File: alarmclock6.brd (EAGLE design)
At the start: 60 x 92 mm, 51 parts, among them Q1 FDN360P, T1 2N2222, X1 MKDSN1,5/2-5,08, X2 MKDSN1,5/2-5,08, X3 MKDSN1,5/2-5,08, X4 MKDSN1,5/2-5,08

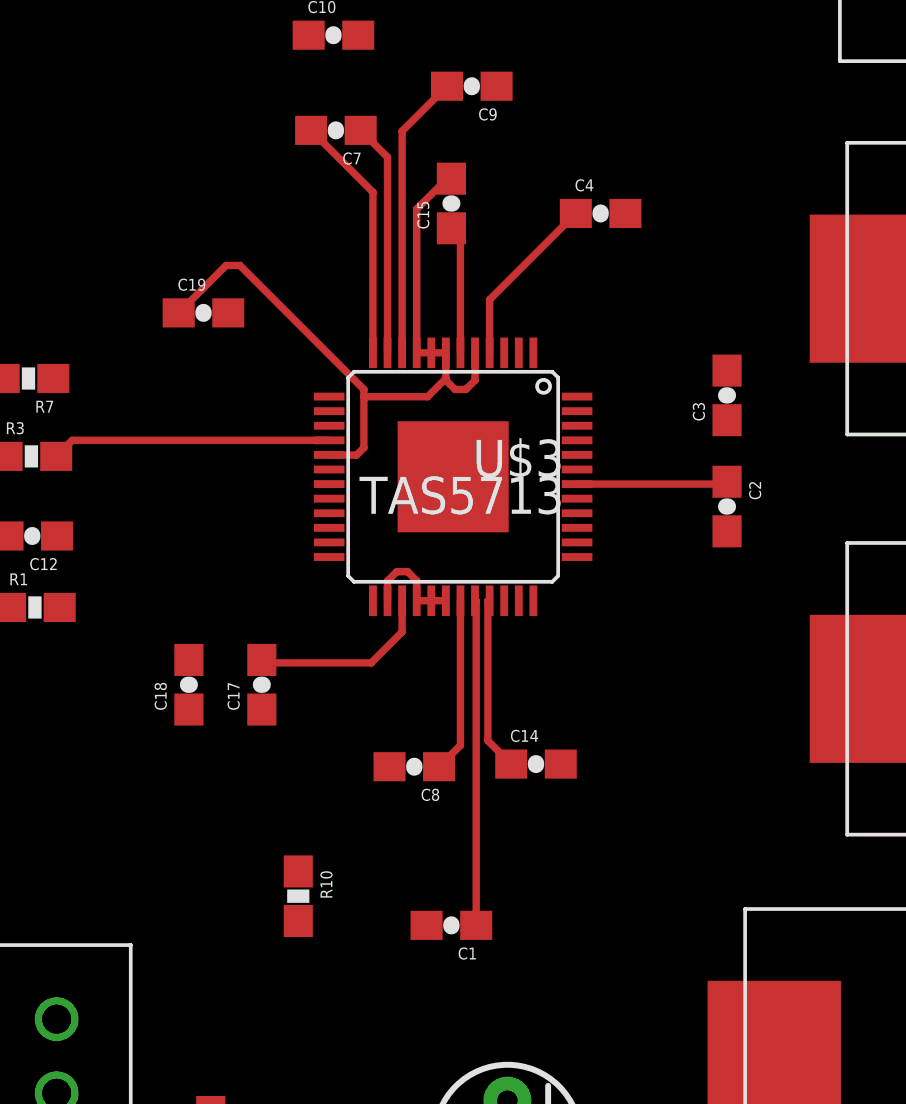
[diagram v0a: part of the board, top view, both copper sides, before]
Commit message: bugfix on DC-DC converter
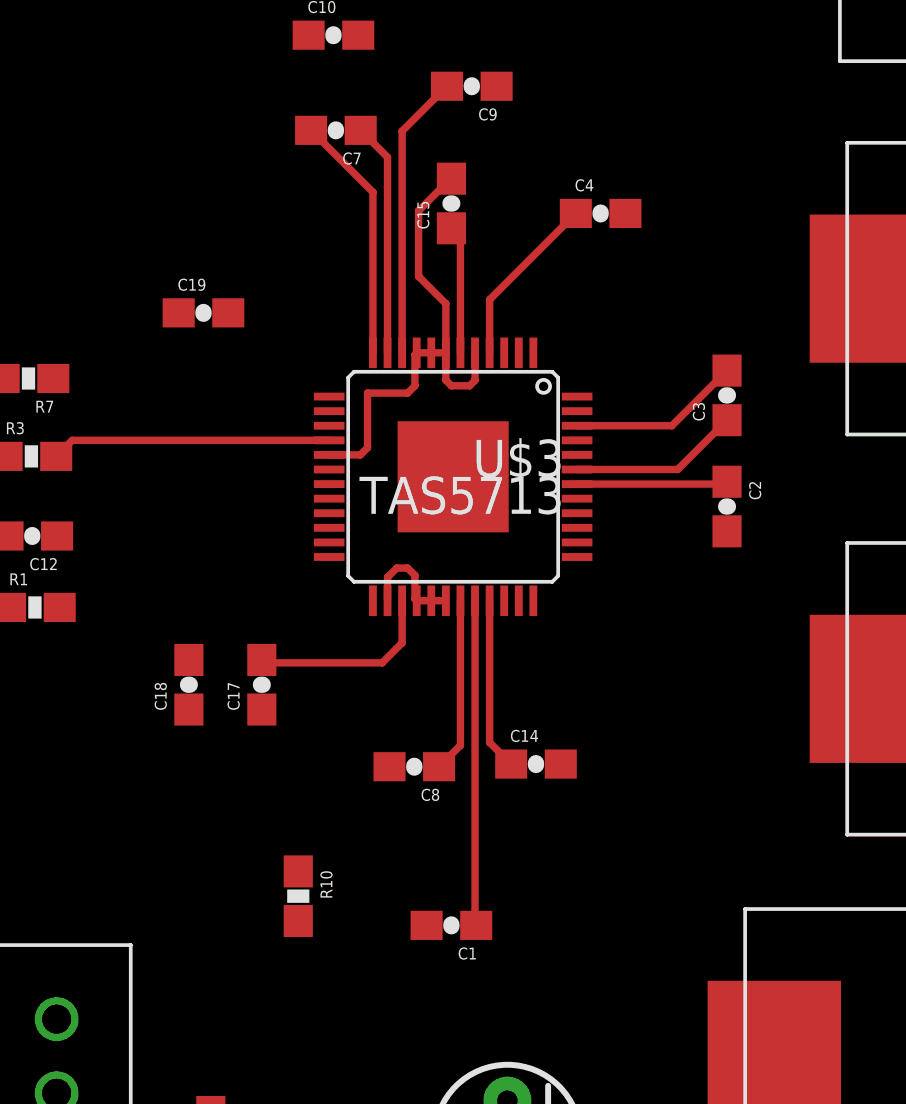
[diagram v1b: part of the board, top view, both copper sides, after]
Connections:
- net N$3: now also U$14.VOUT; no longer U$14.VIN
- net N$43: now also U$14.VIN; no longer U$14.VOUT
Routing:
- net GND: track 29.5 -> 20.9 mm
- net N$14: track 0.00 -> 5.92 mm
- net N$15: track 0.00 -> 5.84 mm
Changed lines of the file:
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@@
 <contactref element="U$4" pad="P$1"/>
 <contactref element="C11" pad="1"/>
-<contactref element="U$14" pad="VIN"/>
-<wire x1="25.17" y1="17.7" x2="5.46" y2="68.75" width="0" layer="19" extent="1-1"/>
+<contactref element="U$14" pad="VOUT"/>
+<wire x1="25.17" y1="17.7" x2="10.54" y2="68.75" width="0" layer="19" extent="1-1"/>
 <wire x1="48.024" y1="13.018" x2="25.17" y2="17.7" width="0" layer="19" extent="1-1"/>
 </signal>
@@
 <contactref element="C11" pad="2"/>
 <contactref element="U$14" pad="GND"/>
-<wire x1="22.06" y1="37.38" x2="22.06" y2="38.065" width="0.254" layer="1"/>
-<wire x1="22.06" y1="38.065" x2="21.75" y2="38.375" width="0.254" layer="1"/>
-<wire x1="21.75" y1="38.375" x2="21.375" y2="38.375" width="0.254" layer="1"/>
-<wire x1="21.375" y1="38.375" x2="21.06" y2="38.06" width="0.254" layer="1"/>
-<wire x1="21.06" y1="38.06" x2="21.06" y2="37.38" width="0.254" layer="1"/>
-<wire x1="23.25" y1="51.85" x2="23.1" y2="51.85" width="0.254" layer="1"/>
-<wire x1="23.1" y1="51.85" x2="22.06" y2="50.81" width="0.254" layer="1"/>
-<wire x1="22.06" y1="50.81" x2="22.06" y2="45.88" width="0.254" layer="1"/>
-<wire x1="23.06" y1="45.88" x2="22.56" y2="45.88" width="0.254" layer="1"/>
-<wire x1="22.56" y1="45.88" x2="22.06" y2="45.88" width="0.254" layer="1"/>
-<wire x1="23.06" y1="45.88" x2="23.06" y2="45" width="0.254" layer="1"/>
-<wire x1="23.06" y1="45" x2="23.06" y2="44.94" width="0.254" layer="1"/>
-<wire x1="23.06" y1="44.94" x2="23.375" y2="44.625" width="0.254" layer="1"/>
-<wire x1="23.375" y1="44.625" x2="23.75" y2="44.625" width="0.254" layer="1"/>
-<wire x1="23.75" y1="44.625" x2="24.06" y2="44.935" width="0.254" layer="1"/>
-<wire x1="24.06" y1="44.935" x2="24.06" y2="45.88" width="0.254" layer="1"/>
-<wire x1="19.06" y1="42.38" x2="19.065" y2="42.375" width="0.254" layer="1"/>
-<wire x1="19.065" y1="42.375" x2="20" y2="42.375" width="0.254" layer="1"/>
-<wire x1="20" y1="42.375" x2="20.25" y2="42.625" width="0.254" layer="1"/>
-<wire x1="20.25" y1="42.625" x2="20.25" y2="44.375" width="0.254" layer="1"/>
-<wire x1="20.25" y1="44.375" x2="22.435" y2="44.375" width="0.254" layer="1"/>
-<wire x1="22.435" y1="44.375" x2="23.06" y2="45" width="0.254" layer="1"/>
 <wire x1="33.6" y1="65.5" x2="37.77" y2="70.5" width="0" layer="19" extent="1-1"/>
 <wire x1="24.8" y1="55.02" x2="33.6" y2="65.5" width="0" layer="19" extent="1-1"/>
 <wire x1="23.25" y1="51.85" x2="24.8" y2="55.02" width="0" layer="19" extent="1-1"/>
-<wire x1="27.56" y1="44.38" x2="24.06" y2="44.935" width="0" layer="19" extent="1-1"/>
+<wire x1="27.56" y1="44.38" x2="24.06" y2="45.88" width="0" layer="19" extent="1-1"/>
 <wire x1="27.56" y1="43.88" x2="27.56" y2="44.38" width="0" layer="19" extent="1-1"/>
-<wire x1="21.375" y1="38.375" x2="20" y2="42.375" width="0" layer="19" extent="1-1"/>
 <wire x1="27.56" y1="39.38" x2="27.56" y2="43.88" width="0" layer="19" extent="1-1"/>
 <wire x1="27.56" y1="38.88" x2="27.56" y2="39.38" width="0" layer="19" extent="1-1"/>
+<wire x1="23.06" y1="37.38" x2="27.56" y2="38.88" width="0" layer="19" extent="1-1"/>
 <wire x1="21.128" y1="31.69" x2="21.06" y2="37.38" width="0" layer="19" extent="1-1"/>
 <wire x1="16.75" y1="33.65" x2="21.128" y2="31.69" width="0" layer="19" extent="1-1"/>
@@
 <wire x1="22.4" y1="26.25" x2="21.128" y2="31.69" width="0" layer="19" extent="1-1"/>
 <wire x1="25.17" y1="20.24" x2="22.4" y2="26.25" width="0" layer="19" extent="1-1"/>
+<wire x1="13.9" y1="47.25" x2="19.06" y2="42.38" width="0" layer="19" extent="1-1"/>
 <wire x1="7.9" y1="45" x2="13.9" y2="47.25" width="0" layer="19" extent="1-1"/>
 <wire x1="8" y1="42.33" x2="7.9" y2="45" width="0" layer="19" extent="1-1"/>
@@
 <wire x1="16.7551" y1="4.579" x2="29.4871" y2="4.579" width="0" layer="19" extent="1-1"/>
 <wire x1="48.024" y1="20.018" x2="25.17" y2="20.24" width="0" layer="19" extent="1-1"/>
-<wire x1="20.25" y1="44.375" x2="20.25" y2="44.625" width="0.254" layer="1"/>
-<wire x1="20.25" y1="44.625" x2="16" y2="48.875" width="0.254" layer="1"/>
-<wire x1="16" y1="48.875" x2="15.525" y2="48.875" width="0.254" layer="1"/>
-<wire x1="15.525" y1="48.875" x2="13.9" y2="47.25" width="0.254" layer="1"/>
-<wire x1="22.06" y1="37.38" x2="22.56" y2="37.38" width="0.254" layer="1"/>
+<wire x1="19.06" y1="42.38" x2="20.13" y2="42.38" width="0.254" layer="1"/>
+<wire x1="20.13" y1="42.38" x2="20.375" y2="42.625" width="0.254" layer="1"/>
+<wire x1="20.375" y1="42.625" x2="20.375" y2="44.5" width="0.254" layer="1"/>
+<wire x1="20.375" y1="44.5" x2="21.75" y2="44.5" width="0.254" layer="1"/>
+<wire x1="21.75" y1="44.5" x2="22" y2="44.75" width="0.254" layer="1"/>
+<wire x1="22" y1="44.75" x2="22" y2="45.82" width="0.254" layer="1"/>
+<wire x1="22" y1="45.82" x2="22.06" y2="45.88" width="0.254" layer="1"/>
+<wire x1="22.56" y1="45.88" x2="22.06" y2="45.88" width="0.254" layer="1"/>
+<wire x1="23.06" y1="45.88" x2="22.56" y2="45.88" width="0.254" layer="1"/>
+<wire x1="23.06" y1="45.88" x2="23.06" y2="44.94" width="0.254" layer="1"/>
+<wire x1="23.06" y1="44.94" x2="23.25" y2="44.75" width="0.254" layer="1"/>
+<wire x1="23.25" y1="44.75" x2="23.875" y2="44.75" width="0.254" layer="1"/>
+<wire x1="23.875" y1="44.75" x2="24.06" y2="44.935" width="0.254" layer="1"/>
+<wire x1="24.06" y1="44.935" x2="24.06" y2="45.88" width="0.254" layer="1"/>
+<wire x1="23.06" y1="45.88" x2="23.06" y2="47.565" width="0.254" layer="1"/>
+<wire x1="23.06" y1="47.565" x2="22.125" y2="48.5" width="0.254" layer="1"/>
+<wire x1="22.125" y1="48.5" x2="22.125" y2="50.75" width="0.254" layer="1"/>
+<wire x1="22.125" y1="50.75" x2="23.225" y2="51.85" width="0.254" layer="1"/>
+<wire x1="23.225" y1="51.85" x2="23.25" y2="51.85" width="0.254" layer="1"/>
+<wire x1="21.06" y1="37.38" x2="21.06" y2="38.185" width="0.254" layer="1"/>
+<wire x1="21.06" y1="38.185" x2="21.375" y2="38.5" width="0.254" layer="1"/>
+<wire x1="21.375" y1="38.5" x2="21.75" y2="38.5" width="0.254" layer="1"/>
+<wire x1="21.75" y1="38.5" x2="22" y2="38.25" width="0.254" layer="1"/>
+<wire x1="22" y1="38.25" x2="22" y2="37.44" width="0.254" layer="1"/>
+<wire x1="22" y1="37.44" x2="22.06" y2="37.38" width="0.254" layer="1"/>
+<wire x1="22.56" y1="37.38" x2="22.06" y2="37.38" width="0.254" layer="1"/>
 <wire x1="22.56" y1="37.38" x2="23.06" y2="37.38" width="0.254" layer="1"/>
 </signal>
@@
 <contactref element="U$3" pad="P$33"/>
 <contactref element="C14" pad="1"/>
-<wire x1="24.56" y1="37.38" x2="24.5" y2="37.38" width="0.254" layer="1"/>
-<wire x1="24.5" y1="37.38" x2="24.5" y2="32.58" width="0.254" layer="1"/>
-<wire x1="24.5" y1="32.58" x2="25.3" y2="31.78" width="0.254" layer="1"/>
+<wire x1="24.56" y1="37.38" x2="24.56" y2="32.52" width="0.254" layer="1"/>
+<wire x1="24.56" y1="32.52" x2="25.3" y2="31.78" width="0.254" layer="1"/>
 </signal>
 <signal name="N$12">
@@
 <contactref element="U$8" pad="P$1"/>
 <wire x1="32.7" y1="45.27" x2="37.82" y2="48.08" width="0" layer="19" extent="1-1"/>
-<wire x1="27.56" y1="43.38" x2="32.7" y2="45.27" width="0" layer="19" extent="1-1"/>
+<wire x1="27.56" y1="43.38" x2="30.81" y2="43.38" width="0.254" layer="1"/>
+<wire x1="30.81" y1="43.38" x2="32.7" y2="45.27" width="0.254" layer="1"/>
 </signal>
 <signal name="N$15">
 <contactref element="U$3" pad="P$43"/>
 <contactref element="C3" pad="1"/>
-<wire x1="27.56" y1="41.88" x2="32.7" y2="43.57" width="0" layer="19" extent="1-1"/>
+<wire x1="27.56" y1="41.88" x2="31.01" y2="41.88" width="0.254" layer="1"/>
+<wire x1="31.01" y1="41.88" x2="32.7" y2="43.57" width="0.254" layer="1"/>
 </signal>
 <signal name="N$16" class="1">
@@
 <wire x1="9.716" y1="10.334" x2="15" y2="18.15" width="0" layer="19" extent="1-1"/>
 <wire x1="4.35" y1="10.334" x2="9.716" y2="10.334" width="0" layer="19" extent="1-1"/>
-<wire x1="21.56" y1="37.38" x2="21.56" y2="36.31" width="0.254" layer="1"/>
-<wire x1="21.56" y1="36.31" x2="20.5" y2="35.25" width="0.254" layer="1"/>
-<wire x1="20.5" y1="35.25" x2="16.85" y2="35.25" width="0.254" layer="1"/>
+<wire x1="21.56" y1="37.38" x2="21.56" y2="35.935" width="0.254" layer="1"/>
+<wire x1="21.56" y1="35.935" x2="20.875" y2="35.25" width="0.254" layer="1"/>
+<wire x1="20.875" y1="35.25" x2="16.85" y2="35.25" width="0.254" layer="1"/>
 <wire x1="16.85" y1="35.25" x2="16.75" y2="35.35" width="0.254" layer="1"/>
 </signal>
@@
 <contactref element="U$3" pad="P$32"/>
 <contactref element="C1" pad="1"/>
-<wire x1="24.06" y1="37.38" x2="24.1" y2="37.38" width="0.254" layer="1"/>
-<wire x1="24.1" y1="37.38" x2="24.1" y2="26.25" width="0.254" layer="1"/>
+<wire x1="24.06" y1="37.38" x2="24.06" y2="26.29" width="0.254" layer="1"/>
+<wire x1="24.06" y1="26.29" x2="24.1" y2="26.25" width="0.254" layer="1"/>
 </signal>
 <signal name="N$39">
@@
 <contactref element="Q1" pad="2"/>
 <contactref element="R11" pad="2"/>
-<contactref element="U$14" pad="VOUT"/>
+<contactref element="U$14" pad="VIN"/>
 <wire x1="26.5" y1="69.65" x2="29.4" y2="69.55" width="0" layer="19" extent="1-1"/>
-<wire x1="10.54" y1="68.75" x2="26.5" y2="69.65" width="0" layer="19" extent="1-1"/>
-<wire x1="8.478" y1="79.612" x2="10.54" y2="68.75" width="0" layer="19" extent="1-1"/>
+<wire x1="8.478" y1="79.612" x2="26.5" y2="69.65" width="0" layer="19" extent="1-1"/>
+<wire x1="5.46" y1="68.75" x2="8.478" y2="79.612" width="0" layer="19" extent="1-1"/>
 </signal>
 </signals>
